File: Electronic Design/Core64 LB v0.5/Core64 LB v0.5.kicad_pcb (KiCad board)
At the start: 2 copper layers, 85 x 170 mm, 146 parts, among them IC1 TPS7A0533PDBVR, IC2 LP3961EMP-5.0, IC3 NCP176AMX330TCG, J1 HEADER_8-PIN_0.1, J10 TSM-106-03-T-DV‎, J11 SSW-116-22-F-S-VS‎, J12 TEENSY Cur. Mon., J13 Core Cur. Mon., J14 SSW-116-22-F-S-VS‎, J17 LED Cur. Mon., J2 HEADER_11-PIN_0.1, J3 Conn_01x08_Female, J4 PRG, J5 HEADER_8-PIN_0.1, J6 HEADER_8-PIN_0.1, J7 S03B-PASK-2_LF__SN_, J8 5V0 Cur. Mon., J9 3V3 Cur. Mon., Q1 MCC_SL3401A, Q10 MMBT4403LT1G, Q11 MMBT4403LT1G, Q12 MMBT4401LT1G, Q13 MMBT4403LT1G, Q14 MMBT4403LT1G, Q15 MMBT4401LT1G, Q16 MMBT4403LT1G, Q17 MMBT4403LT1G, Q18 MMBT4401LT1G, Q19 MMBT4401LT1G, Q2 MMBT4403LT1G, Q20 MMBT4401LT1G, Q21 MMBT4401LT1G, Q22 Q_NMOS_DGS_NVTR4503NT1G, Q3 MMBT4403LT1G, Q4 MMBT4403LT1G, Q5 MMBT4403LT1G, Q6 MMBT4401LT1G, Q7 MMBT4401LT1G, Q8 MMBT4401LT1G, Q9 MMBT4401LT1G, SW1 JS102011SAQN, U1 74HC02, U2 Teensy3.2, U3 SN74LV1T125DBVR, U4 M24C01-RMN, U5 74HC238, U6 Micro_LiPo_Charger, U7 LM393, U8 Adafruit_3.2_TFT_1743, X1 QWIIC, X2 Header_9-PIN_0.1, X3 SAO_conn_SFH11-NBPC-D03-ST-BK, X4 SSW-104-22-L-S-VS

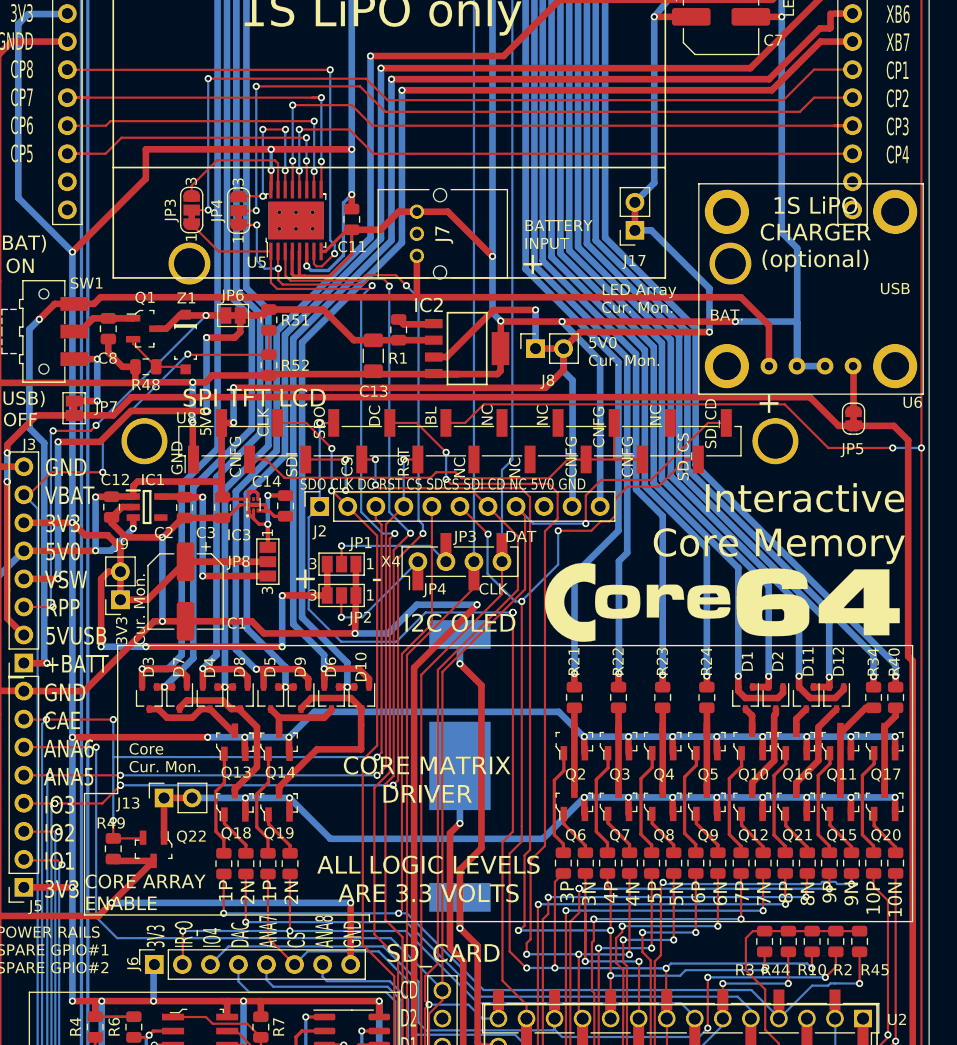
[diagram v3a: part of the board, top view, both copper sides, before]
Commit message: LB Layout refinement for optional hall switches
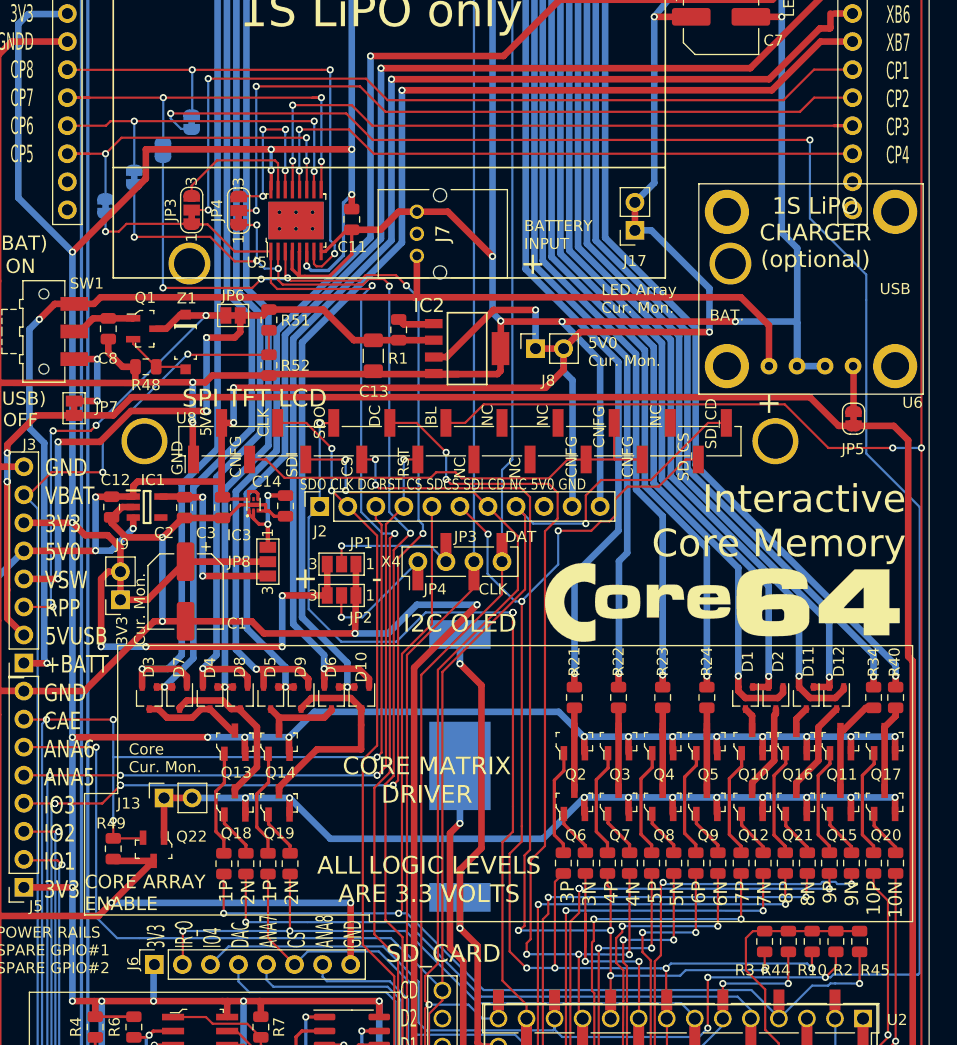
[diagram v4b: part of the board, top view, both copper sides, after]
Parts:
- added JP10: Hall Switch 2, Jumper:SolderJumper-2_P1.3mm_Bridged_RoundedPad1.0x1.5mm, B.Cu at (-29.5, 21.2)
- added JP11: Hall Switch 3, Jumper:SolderJumper-2_P1.3mm_Bridged_RoundedPad1.0x1.5mm, B.Cu at (-26.9, 18.7)
- added JP12: Hall Switch 4, Jumper:SolderJumper-2_P1.3mm_Bridged_RoundedPad1.0x1.5mm, B.Cu at (-24.3, 16.2)
- added JP9: Hall Switch 1, Jumper:SolderJumper-2_P1.3mm_Bridged_RoundedPad1.0x1.5mm, B.Cu at (-32.1, 23.8)
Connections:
- net SAO_G1_or_SPARE_1_or_CP_ADDR_0 renamed HS1
- net SAO_G2_or_SPARE_2_or_CP_ADDR_1 renamed HS2
- net SPARE_3_or_CP_ADDR_2 renamed HS3
- net SPARE_4_IR_IN renamed HS4
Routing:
- net HS4: track 73.3 -> 223.2 mm, vias 3 -> 5
- net HS3: track 180.1 -> 203.6 mm, vias 7 -> 10
- net HS2: track 268.6 -> 285.4 mm, vias 10 -> 12
- net HS1: track 262.7 -> 272.5 mm, vias 8 -> 9
- net CP6_EN: track 28.7 -> 33.2 mm, vias 2 -> 3
- net CP8_EN: track 44.2 -> 48.3 mm, vias 2 -> 3
- net CP5_EN: track 29.0 -> 33.1 mm, vias 2 -> 3
- net CP7_EN: track 34.2 -> 38.3 mm, vias 2 -> 3
- net -BATT: track 903.2 -> 902.4 mm

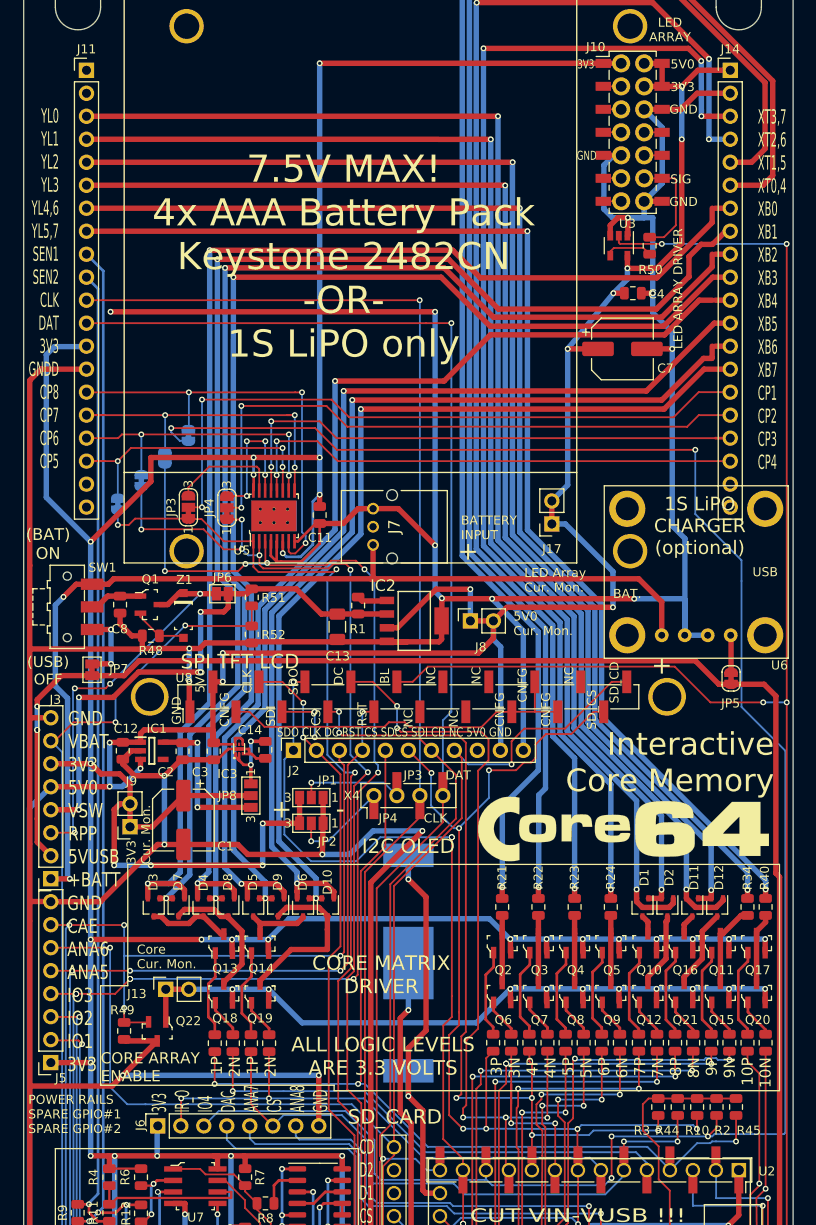
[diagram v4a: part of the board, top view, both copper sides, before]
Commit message: Connect row-col-0 to analog inputs for self-test mode
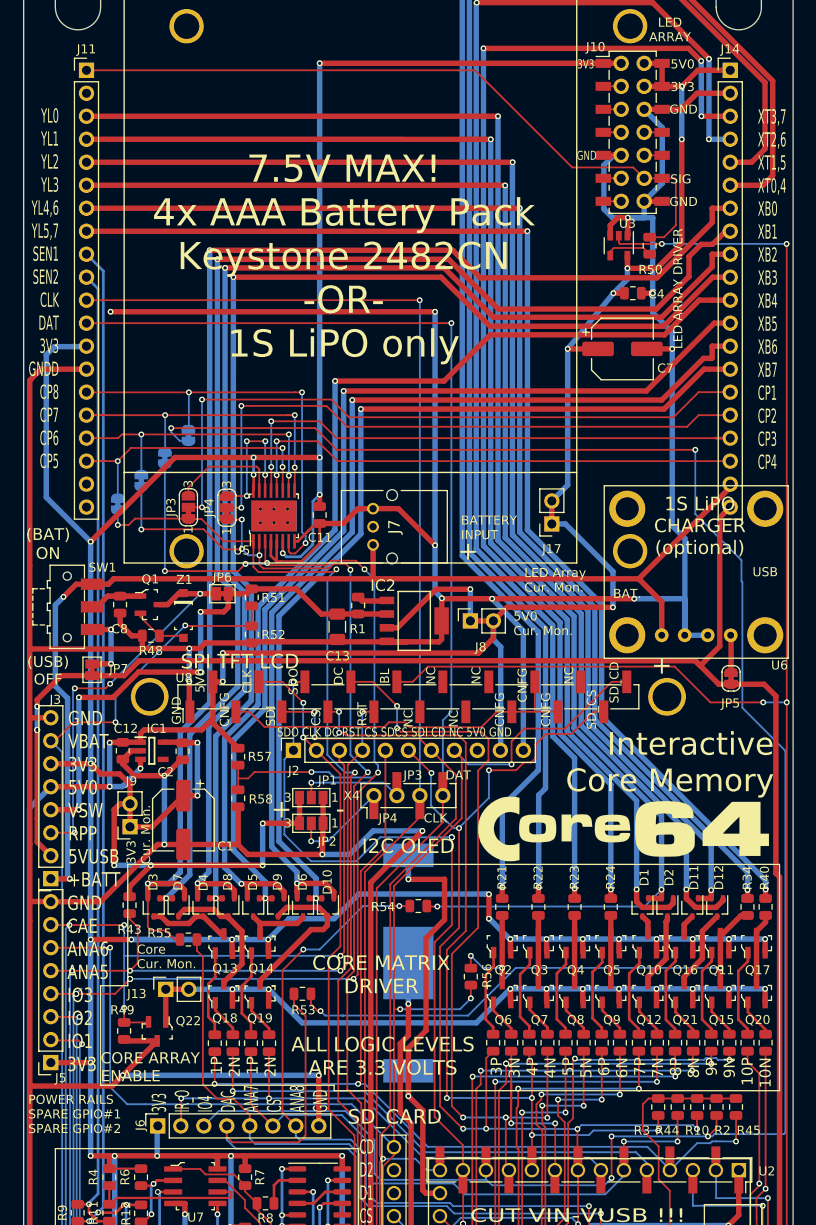
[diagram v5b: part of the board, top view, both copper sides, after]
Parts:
- removed C14, C3: 1uF, Capacitor_SMD:C_0805_2012Metric
- removed IC3: NCP176AMX330TCG, NCP176AMX330TCG:NCP176AMX330TCG
- removed JP8: 3V3_Select, Jumper:SolderJumper-3_P1.3mm_Open_Pad1.0x1.5mm_NumberLabels
- added R43: 10k, Resistor_SMD:R_0805_2012Metric, F.Cu at (-30.8, 68.1)
- added R53: 10k, Resistor_SMD:R_0805_2012Metric, F.Cu at (-11.7, 77.9)
- added R54: 10k, Resistor_SMD:R_0805_2012Metric, F.Cu at (1.10, 68.2)
- added R55: 10k, Resistor_SMD:R_0805_2012Metric, F.Cu at (-24.3, 71.9)
- added R56: 10k, Resistor_SMD:R_0805_2012Metric, F.Cu at (6.90, 76.0)
- added R57: 11k, Resistor_SMD:R_0805_2012Metric, F.Cu at (-18.8, 51.7)
- added R58: 11k, Resistor_SMD:R_0805_2012Metric, F.Cu at (-18.8, 56.3)
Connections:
- net HS3 renamed 5V0_MON
- net Net-(Q11-Pad3) renamed RR0_MON
- net Net-(Q2-Pad3) renamed TC0_MON
- net XB0 renamed BC0_MON
- net YL0 renamed LR0_MON
- C2 pad 1: Net-(C2-Pad1) -> 3V3
- IC1 pad 5: Net-(C2-Pad1) -> 3V3
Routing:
- net LED_ARRAY_5V0_SIG: track 12.1 -> 78.6 mm
- net RR0_MON: track 9.33 -> 58.5 mm, vias 0 -> 2
- net SPARE_ANA_8: track 45.9 -> 80.7 mm, vias 1 -> 3
- net LR0_MON: track 140.8 -> 167.5 mm, vias 2 -> 3
- net SPARE_ADC_DAC: track 39.0 -> 65.6 mm
- net SPARE_ANA_7: track 49.2 -> 73.3 mm
- net 5V0_MON: track 203.6 -> 223.4 mm, vias 10 -> 11
- net TEENSY_VUSB: track 176.4 -> 196.0 mm
- net 3V3: track 565.9 -> 584.1 mm, vias 35 -> 39
- net Net-(C2-Pad1): track 16.9 -> 0.00 mm, vias 2 -> 0
- net +BATT: track 110.8 -> 125.4 mm
- net SD_SPI_CD: track 168.3 -> 178.7 mm, vias 3 -> 5
- net Net-(C14-Pad1): track 9.45 -> 0.00 mm, vias 2 -> 0
- net BC0_MON: track 143.6 -> 151.2 mm
- net SPARE_5: track 154.2 -> 161.3 mm
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
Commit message: LB layout redlines
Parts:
- SW1: footprint Button_Switch_SMD:SW_SPDT_CK-JS102011SAQN -> Button_Switch_SMD:SW_SPDT_CK-JS102011SAQN_Core64_Recessed
- U5: footprint Digikey:TSSOP-16-1EP_W4.40mm -> Digikey:TSSOP-16-W4.40mm
- moved J6 0.76 mm to (-27.7, 93.2)
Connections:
- net VBAT_MON renamed BAT_MON
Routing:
- net SPARE_ADC_DAC: track 65.6 -> 63.9 mm
- net IR_OUT: track 59.7 -> 61.2 mm
- net TEENSY_VUSB: track 196.0 -> 194.7 mm
- net Q2P: track 68.0 -> 68.8 mm
- net XB2: track 139.7 -> 138.9 mm
- net 3V3: track 584.1 -> 583.3 mm
- net XB6: track 110.1 -> 109.3 mm
- net +BATT: track 125.4 -> 124.7 mm
- net HS4: track 223.2 -> 223.9 mm
- net -BATT: track 895.5 -> 896.2 mm
- net +RPP: track 43.8 -> 43.3 mm
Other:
- outline, holes or cut-outs redrawn
- board text added: "1P 1N 2P 2N"
- board text added: "3V3 IR_O IO4 DAC ANA7 T_CS ANA8 GND"
- board text added: "GND BMON 3V3 5V0 VSW RPP 5VUSB +BATT"
- board text added: "GND CAE ANA6 IO5 IO3 IO2 IO1 3V3"
- board text added: "OFF (USB)"
- board text removed: "(USB) OFF"
- board text removed: "1P 2N 1P 2N"
- board text removed: "3V3 IR_O IO4 DAC ANA7 CS ANA8 GND"
- board text removed: "GND CAE ANA6 ANA5 IO3 IO2 IO1 3V3"
- board text removed: "GND VBAT 3V3 5V0 VSW RPP 5VUSB +BATT"

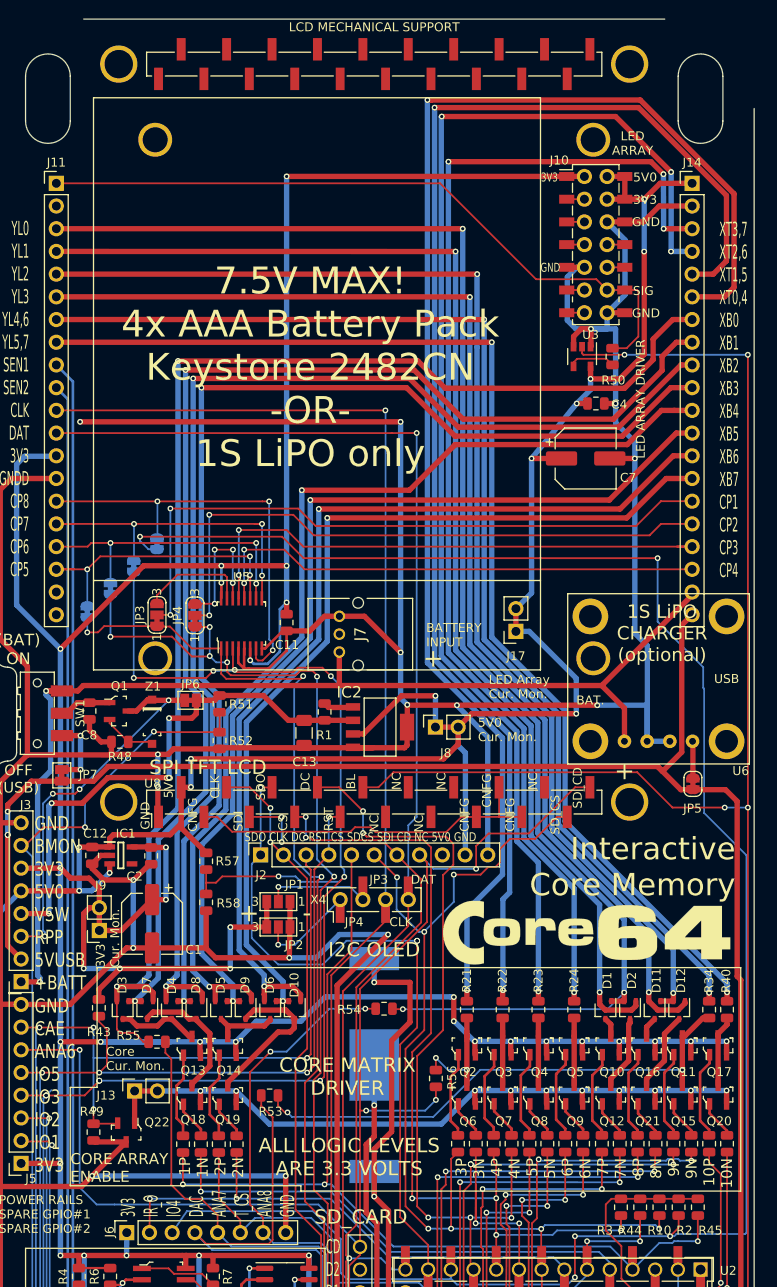
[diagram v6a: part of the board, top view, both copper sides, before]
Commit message: Move LiPo Charger to top edge, increase LCD footprint top header edge up 1mm
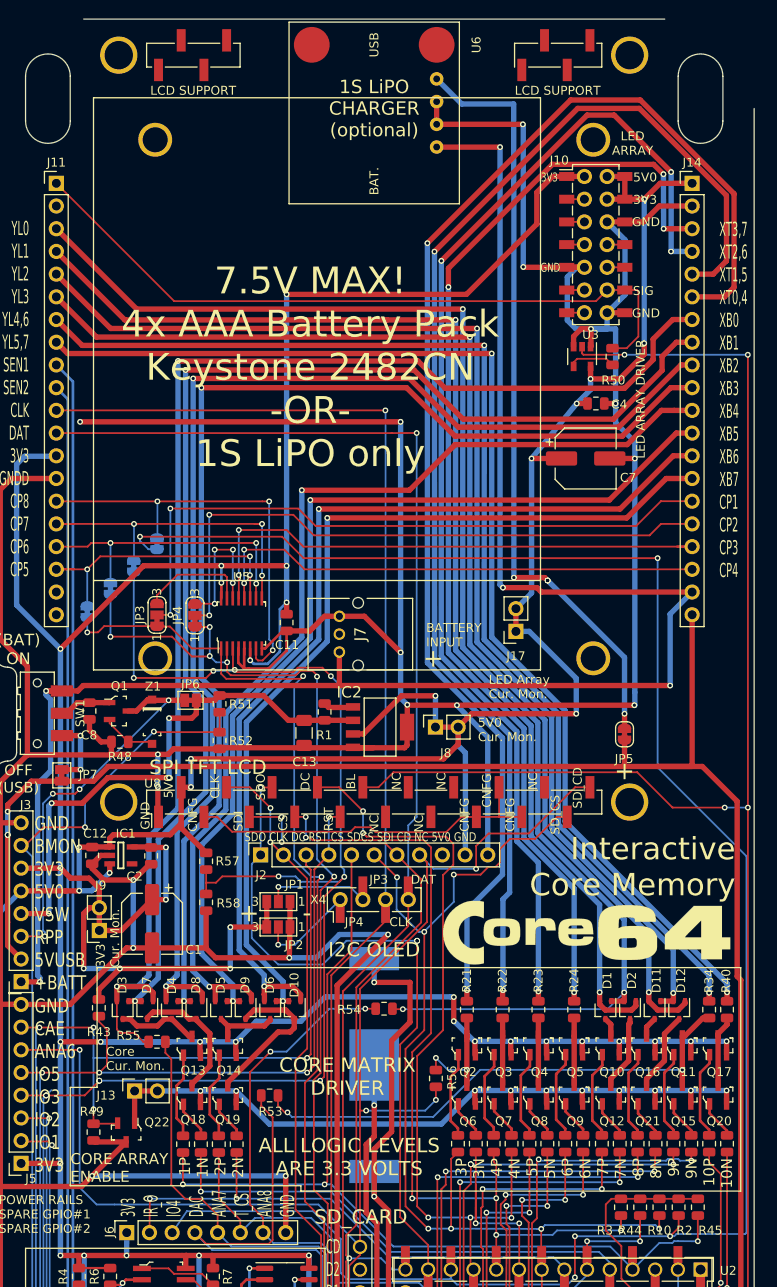
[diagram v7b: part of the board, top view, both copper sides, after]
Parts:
- U6: footprint Core_Memory_8x8_Array:Micro_LiPo_Charger -> Core_Memory_8x8_Array:Micro_LiPo_Charger_CornerSMD
- moved U6 70.8 mm to (0.00, -32.0), turned to 270 degrees
- moved JP5 9.45 mm to (28.0, 37.5)
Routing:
- net Net-(JP5-Pad2): track 4.13 -> 86.8 mm, vias 0 -> 4
- net +BATT: track 124.7 -> 200.1 mm, vias 2 -> 5
- net -BATT: track 896.2 -> 918.5 mm, vias 31 -> 33
- net XT1,5: track 152.3 -> 142.8 mm
- net XT0,4: track 160.2 -> 150.8 mm
- net XT2,6: track 143.0 -> 133.7 mm
- net XT3,7: track 133.7 -> 126.5 mm
- net 3V3: track 583.3 -> 577.7 mm
- net LR0_MON: track 167.5 -> 162.3 mm
- net YL1: track 140.6 -> 136.1 mm
- net TEENSY_VUSB: track 194.7 -> 198.9 mm
- net YL2: track 138.9 -> 135.4 mm
- net YL3: track 138.3 -> 135.7 mm
- net YL4: track 134.6 -> 132.9 mm
- net LED_ARRAY_5V0_SIG: track 78.6 -> 79.6 mm
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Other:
- board text added: "LCD SUPPORT"
- board text removed: "LCD MECHANICAL SUPPORT"
